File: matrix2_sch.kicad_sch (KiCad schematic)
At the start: 166 parts, among them SW10 SW_Push, SW11 SW_Push, SW12 SW_Push, SW13 SW_Push, SW14 SW_Push, SW15 SW_Push, SW16 SW_Push, SW17 SW_Push, SW18 SW_Push, SW19 SW_Push, SW2 RotaryEncoder_Switch, SW20 SW_Push, SW21 SW_Push, SW22 SW_Push, SW23 SW_Push, SW24 SW_Push, SW25 SW_Push, SW26 SW_Push, SW27 SW_Push, SW28 SW_Push, SW29 SW_Push, SW3 SW_Push, SW30 SW_Push, SW31 SW_Push, SW32 SW_Push, SW33 SW_Push, SW34 SW_Push, SW35 SW_Push, SW36 SW_Push, SW37 SW_Push, SW38 SW_Push, SW39 SW_Push, SW4 SW_Push, SW40 SW_Push, SW41 SW_Push, SW42 SW_Push, SW43 SW_Push, SW44 SW_Push, SW45 SW_Push, SW46 SW_Push, SW47 SW_Push, SW48 SW_Push, SW49 SW_Push, SW5 SW_Push, SW50 SW_Push, SW51 SW_Push, SW52 SW_Push, SW53 SW_Push, SW54 SW_Push, SW55 SW_Push, SW56 SW_Push, SW57 SW_Push, SW58 SW_Push, SW59 SW_Push, SW6 SW_Push, SW60 SW_Push, SW61 SW_Push, SW62 SW_Push, SW63 SW_Push, SW64 SW_Push, SW65 SW_Push, SW66 SW_Push, SW67 SW_Push, SW68 SW_Push, SW69 SW_Push, SW7 SW_Push, SW70 SW_Push, SW71 SW_Push, SW72 SW_Push, SW73 SW_Push, SW74 SW_Push, SW75 SW_Push, SW76 SW_Push, SW77 SW_Push, SW78 SW_Push, SW79 SW_Push, SW8 SW_Push, SW80 SW_Push, SW81 SW_Push, SW82 SW_Push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

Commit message: changed to 60 :C
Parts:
- removed D162, D163, D164, D165, D166, D167, D168, D169, D170, D171, D172, D173, D174, D175, D176: D_Small, Diode_SMD:D_SOD-123, symbol Device:D_Small
- removed SW70, SW71, SW73, SW74, SW79, SW80, SW81, SW82, SW83, SW84: SW_Push, acheron_MXH:MX100H, symbol Switch:SW_Push
- removed SW72: SW_Push, acheron_MXH:MX175H, symbol Switch:SW_Push
- removed SW75, SW76, SW77: SW_Push, acheron_MXH:MX125H, symbol Switch:SW_Push
- removed SW78: SW_Push, acheron_MXH:MX625HR, symbol Switch:SW_Push
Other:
- moved on the sheet: D100, D101, D102, D103, D104, D105, D106, D107, D108, D109, D110, D111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

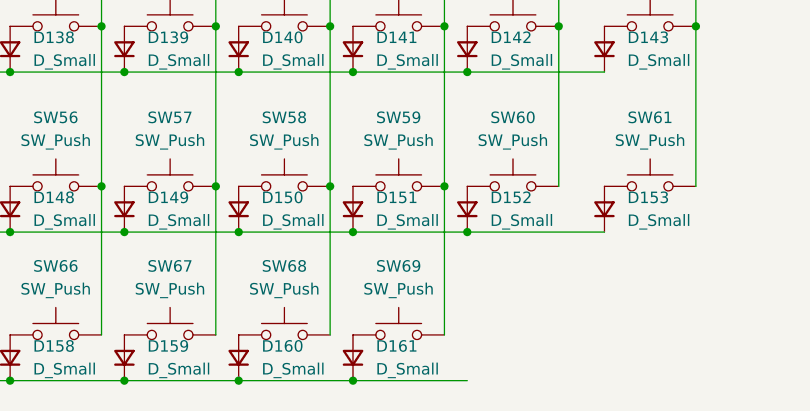
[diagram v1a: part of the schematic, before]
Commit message: moved keys/neopixels
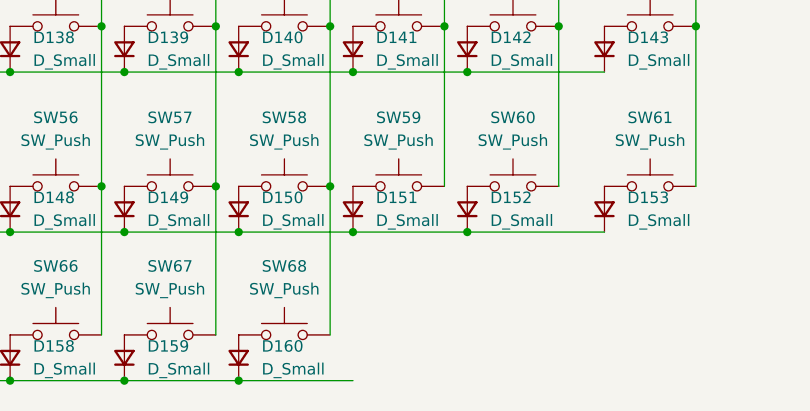
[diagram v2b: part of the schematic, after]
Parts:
- removed D161: D_Small, Diode_SMD:D_SOD-123, symbol Device:D_Small
- removed SW69: SW_Push, acheron_MXH:MX100H, symbol Switch:SW_Push
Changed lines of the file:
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@@
   (junction (at 166.37 87.63) (diameter 0) (color 0 0 0 0)
   )
-  (junction (at 128.27 165.1) (diameter 0) (color 0 0 0 0)
-  )
   (junction (at 64.77 74.93) (diameter 0) (color 0 0 0 0)
   )
@@
   (junction (at 125.73 69.85) (diameter 0) (color 0 0 0 0)
   )
-  (junction (at 138.43 143.51) (diameter 0) (color 0 0 0 0)
-  )
   (junction (at 87.63 143.51) (diameter 0) (color 0 0 0 0)
   )
@@
     (stroke (width 0) (type default) (color 0 0 0 0))
   )
-  (wire (pts (xy 138.43 143.51) (xy 138.43 160.02))
-    (stroke (width 0) (type default) (color 0 0 0 0))
-  )
   (wire (pts (xy 30.48 110.49) (xy 39.37 110.49))
     (stroke (width 0) (type default) (color 0 0 0 0))
@@
   )
   (wire (pts (xy 166.37 87.63) (xy 166.37 105.41))
-    (stroke (width 0) (type default) (color 0 0 0 0))
-  )
-  (wire (pts (xy 128.27 165.1) (xy 140.97 165.1))
     (stroke (width 0) (type default) (color 0 0 0 0))
   )
@@
     )
     (property "Datasheet" "~" (id 3) (at 77.47 90.17 90)
-      (effects (font (size 1.27 1.27)) hide)
-    )
-    (pin "1")
-    (pin "2")
-  )
-  (symbol (lib_id "Device:D_Small") (at 128.27 162.56 90) (unit 1)
-    (in_bom yes) (on_board yes)
-    (property "Reference" "D161" (id 0) (at 130.81 161.29 90)
-      (effects (font (size 1.27 1.27)) (justify right))
-    )
-    (property "Value" "D_Small" (id 1) (at 130.81 163.83 90)
-      (effects (font (size 1.27 1.27)) (justify right))
-    )
-    (property "Footprint" "Diode_SMD:D_SOD-123" (id 2) (at 128.27 162.56 90)
-      (effects (font (size 1.27 1.27)) hide)
-    )
-    (property "Datasheet" "~" (id 3) (at 128.27 162.56 90)
       (effects (font (size 1.27 1.27)) hide)
     )
@@
       (effects (font (size 1.27 1.27)) hide)
     )
-    (pin "1")
-    (pin "2")
-  )
-  (symbol (lib_id "Switch:SW_Push") (at 133.35 160.02 0) (unit 1)
-    (in_bom yes) (on_board yes) (fields_autoplaced)
-    (property "Reference" "SW69" (id 0) (at 133.35 152.4 0))
-    (property "Value" "SW_Push" (id 1) (at 133.35 154.94 0))
-    (property "Footprint" "acheron_MXH:MX100H" (id 2) (at 133.35 154.94 0)
-      (effects (font (size 1.27 1.27)) hide)
-    )
-    (property "Datasheet" "~" (id 3) (at 133.35 154.94 0)
-      (effects (font (size 1.27 1.27)) hide)
-    )

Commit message: strange short?
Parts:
- SW16: footprint acheron_MXH:MX100H -> acheron_MXH:MX200HR
- SW17: footprint acheron_MXH:MX100H -> acheron_MXH:MX150H
- SW30: footprint acheron_MXH:MX200HR -> acheron_MXH:MX150H
- SW32: footprint acheron_MXH:MX150H -> acheron_MXH:MX175H
- SW44, SW46: footprint acheron_MXH:MX100H -> acheron_MXH:MX225HR
- SW45: footprint acheron_MXH:MX150H -> acheron_MXH:MX100H
- SW47: footprint acheron_MXH:MX175H -> acheron_MXH:MX100H
- SW57: footprint acheron_MXH:MX100H -> acheron_MXH:MX175H
- SW59: footprint acheron_MXH:MX225HR -> acheron_MXH:MX100H
- SW60, SW62, SW64, SW65: footprint acheron_MXH:MX100H -> acheron_MXH:MX125H
- SW61: footprint acheron_MXH:MX225HR -> acheron_MXH:MX125H
- SW63: footprint acheron_MXH:MX100H -> acheron_MXH:MX625HR
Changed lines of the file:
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@@
     (property "Reference" "SW64" (id 0) (at 69.85 152.4 0))
     (property "Value" "SW_Push" (id 1) (at 69.85 154.94 0))
-    (property "Footprint" "acheron_MXH:MX100H" (id 2) (at 69.85 154.94 0)
+    (property "Footprint" "acheron_MXH:MX125H" (id 2) (at 69.85 154.94 0)
       (effects (font (size 1.27 1.27)) hide)
     )
@@
     (property "Reference" "SW61" (id 0) (at 161.29 135.89 0))
     (property "Value" "SW_Push" (id 1) (at 161.29 138.43 0))
-    (property "Footprint" "acheron_MXH:MX225HR" (id 2) (at 161.29 138.43 0)
+    (property "Footprint" "acheron_MXH:MX125H" (id 2) (at 161.29 138.43 0)
       (effects (font (size 1.27 1.27)) hide)
     )
@@
     (property "Reference" "SW45" (id 0) (at 82.55 118.11 0))
     (property "Value" "SW_Push" (id 1) (at 82.55 120.65 0))
-    (property "Footprint" "acheron_MXH:MX150H" (id 2) (at 82.55 120.65 0)
+    (property "Footprint" "acheron_MXH:MX100H" (id 2) (at 82.55 120.65 0)
       (effects (font (size 1.27 1.27)) hide)
     )
@@
     (property "Reference" "SW47" (id 0) (at 107.95 118.11 0))
     (property "Value" "SW_Push" (id 1) (at 107.95 120.65 0))
-    (property "Footprint" "acheron_MXH:MX175H" (id 2) (at 107.95 120.65 0)
+    (property "Footprint" "acheron_MXH:MX100H" (id 2) (at 107.95 120.65 0)
       (effects (font (size 1.27 1.27)) hide)
     )
@@
     (property "Reference" "SW44" (id 0) (at 69.85 118.11 0))
     (property "Value" "SW_Push" (id 1) (at 69.85 120.65 0))
-    (property "Footprint" "acheron_MXH:MX100H" (id 2) (at 69.85 120.65 0)
+    (property "Footprint" "acheron_MXH:MX225HR" (id 2) (at 69.85 120.65 0)
       (effects (font (size 1.27 1.27)) hide)
     )
@@
     (property "Reference" "SW63" (id 0) (at 57.15 152.4 0))
     (property "Value" "SW_Push" (id 1) (at 57.15 154.94 0))
-    (property "Footprint" "acheron_MXH:MX100H" (id 2) (at 57.15 154.94 0)
+    (property "Footprint" "acheron_MXH:MX625HR" (id 2) (at 57.15 154.94 0)
       (effects (font (size 1.27 1.27)) hide)
     )
@@
     (property "Reference" "SW32" (id 0) (at 44.45 97.79 0))
     (property "Value" "SW_Push" (id 1) (at 44.45 100.33 0))
-    (property "Footprint" "acheron_MXH:MX150H" (id 2) (at 44.45 100.33 0)
+    (property "Footprint" "acheron_MXH:MX175H" (id 2) (at 44.45 100.33 0)
       (effects (font (size 1.27 1.27)) hide)
     )
@@
     (property "Reference" "SW62" (id 0) (at 44.45 152.4 0))
     (property "Value" "SW_Push" (id 1) (at 44.45 154.94 0))
-    (property "Footprint" "acheron_MXH:MX100H" (id 2) (at 44.45 154.94 0)
+    (property "Footprint" "acheron_MXH:MX125H" (id 2) (at 44.45 154.94 0)
       (effects (font (size 1.27 1.27)) hide)
     )
@@
     (property "Reference" "SW60" (id 0) (at 146.05 135.89 0))
     (property "Value" "SW_Push" (id 1) (at 146.05 138.43 0))
-    (property "Footprint" "acheron_MXH:MX100H" (id 2) (at 146.05 138.43 0)
+    (property "Footprint" "acheron_MXH:MX125H" (id 2) (at 146.05 138.43 0)
       (effects (font (size 1.27 1.27)) hide)
     )
@@
     (property "Reference" "SW17" (id 0) (at 107.95 62.23 0))
     (property "Value" "SW_Push" (id 1) (at 107.95 64.77 0))
-    (property "Footprint" "acheron_MXH:MX100H" (id 2) (at 107.95 64.77 0)
+    (property "Footprint" "acheron_MXH:MX150H" (id 2) (at 107.95 64.77 0)
       (effects (font (size 1.27 1.27)) hide)
     )
@@
     (property "Reference" "SW16" (id 0) (at 95.25 62.23 0))
     (property "Value" "SW_Push" (id 1) (at 95.25 64.77 0))
-    (property "Footprint" "acheron_MXH:MX100H" (id 2) (at 95.25 64.77 0)
+    (property "Footprint" "acheron_MXH:MX200HR" (id 2) (at 95.25 64.77 0)
       (effects (font (size 1.27 1.27)) hide)
     )
@@
     (property "Reference" "SW30" (id 0) (at 146.05 80.01 0))
     (property "Value" "SW_Push" (id 1) (at 146.05 82.55 0))
-    (property "Footprint" "acheron_MXH:MX200HR" (id 2) (at 146.05 82.55 0)
+    (property "Footprint" "acheron_MXH:MX150H" (id 2) (at 146.05 82.55 0)
       (effects (font (size 1.27 1.27)) hide)
     )
@@
     (property "Reference" "SW65" (id 0) (at 82.55 152.4 0))
     (property "Value" "SW_Push" (id 1) (at 82.55 154.94 0))
-    (property "Footprint" "acheron_MXH:MX100H" (id 2) (at 82.55 154.94 0)
+    (property "Footprint" "acheron_MXH:MX125H" (id 2) (at 82.55 154.94 0)
       (effects (font (size 1.27 1.27)) hide)
     )
@@
     (property "Reference" "SW59" (id 0) (at 133.35 135.89 0))
     (property "Value" "SW_Push" (id 1) (at 133.35 138.43 0))
-    (property "Footprint" "acheron_MXH:MX225HR" (id 2) (at 133.35 138.43 0)
+    (property "Footprint" "acheron_MXH:MX100H" (id 2) (at 133.35 138.43 0)
       (effects (font (size 1.27 1.27)) hide)
     )
@@
     (property "Reference" "SW46" (id 0) (at 95.25 118.11 0))
     (property "Value" "SW_Push" (id 1) (at 95.25 120.65 0))
-    (property "Footprint" "acheron_MXH:MX100H" (id 2) (at 95.25 120.65 0)
+    (property "Footprint" "acheron_MXH:MX225HR" (id 2) (at 95.25 120.65 0)
       (effects (font (size 1.27 1.27)) hide)
     )
@@
     (property "Reference" "SW57" (id 0) (at 107.95 135.89 0))
     (property "Value" "SW_Push" (id 1) (at 107.95 138.43 0))
-    (property "Footprint" "acheron_MXH:MX100H" (id 2) (at 107.95 138.43 0)
-      (effects (font (size 1.27 1.27)) hide)
-    )
+    (property "Footprint" "acheron_MXH:MX175H" (id 2) (at 107.95 138.43 0)
+      (effects (font (size 1.27 1.27)) hide)
+    )

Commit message: began routing for real
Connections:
- net +5V renamed GND
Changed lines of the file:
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@@
     (pin "2")
   )
-  (symbol (lib_id "keyboard_parts:GND") (at 203.2 53.34 0) (unit 1)
+  (symbol (lib_id "power:GND") (at 203.2 53.34 0) (unit 1)
     (in_bom yes) (on_board yes)
-    (property "Reference" "#PWR0211" (id 0) (at 203.2 52.07 0)
-      (effects (font (size 0.508 0.508)) hide)
+    (property "Reference" "#PWR0205" (id 0) (at 203.2 59.69 0)
+      (effects (font (size 1.27 1.27)) hide)
     )
     (property "Value" "GND" (id 1) (at 203.2 55.88 0)
@@
     )
     (property "Footprint" "" (id 2) (at 203.2 53.34 0)
-      (effects (font (size 1.524 1.524)))
+      (effects (font (size 1.27 1.27)) hide)
     )
     (property "Datasheet" "" (id 3) (at 203.2 53.34 0)
-      (effects (font (size 1.524 1.524)))
+      (effects (font (size 1.27 1.27)) hide)
     )
     (pin "1")

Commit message: fixed edges
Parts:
- SW16: footprint acheron_MXH:MX200HR -> acheron_MXH:MX200H
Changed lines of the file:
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@@
     (property "Reference" "SW16" (id 0) (at 95.25 62.23 0))
     (property "Value" "SW_Push" (id 1) (at 95.25 64.77 0))
-    (property "Footprint" "acheron_MXH:MX200HR" (id 2) (at 95.25 64.77 0)
+    (property "Footprint" "acheron_MXH:MX200H" (id 2) (at 95.25 64.77 0)
       (effects (font (size 1.27 1.27)) hide)
     )

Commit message: fked up LEDs :C
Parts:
- SW16: footprint acheron_MXH:MX200H -> acheron_MXH:MX200HR
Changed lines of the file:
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@@
     (property "Reference" "SW16" (id 0) (at 95.25 62.23 0))
     (property "Value" "SW_Push" (id 1) (at 95.25 64.77 0))
-    (property "Footprint" "acheron_MXH:MX200H" (id 2) (at 95.25 64.77 0)
+    (property "Footprint" "acheron_MXH:MX200HR" (id 2) (at 95.25 64.77 0)
       (effects (font (size 1.27 1.27)) hide)
     )
